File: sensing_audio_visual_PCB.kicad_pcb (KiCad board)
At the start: 2 copper layers, 52 x 41.4 mm, 0 parts

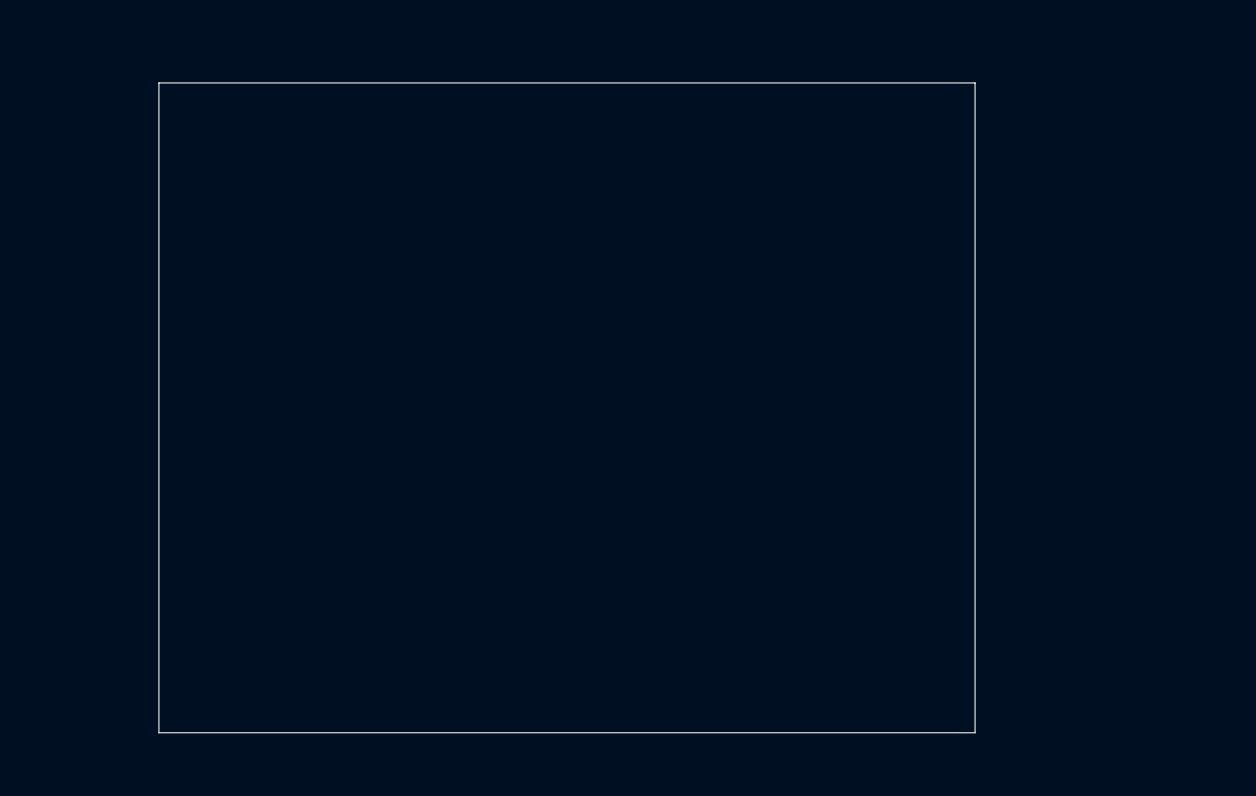
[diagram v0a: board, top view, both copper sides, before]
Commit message: Footprints added
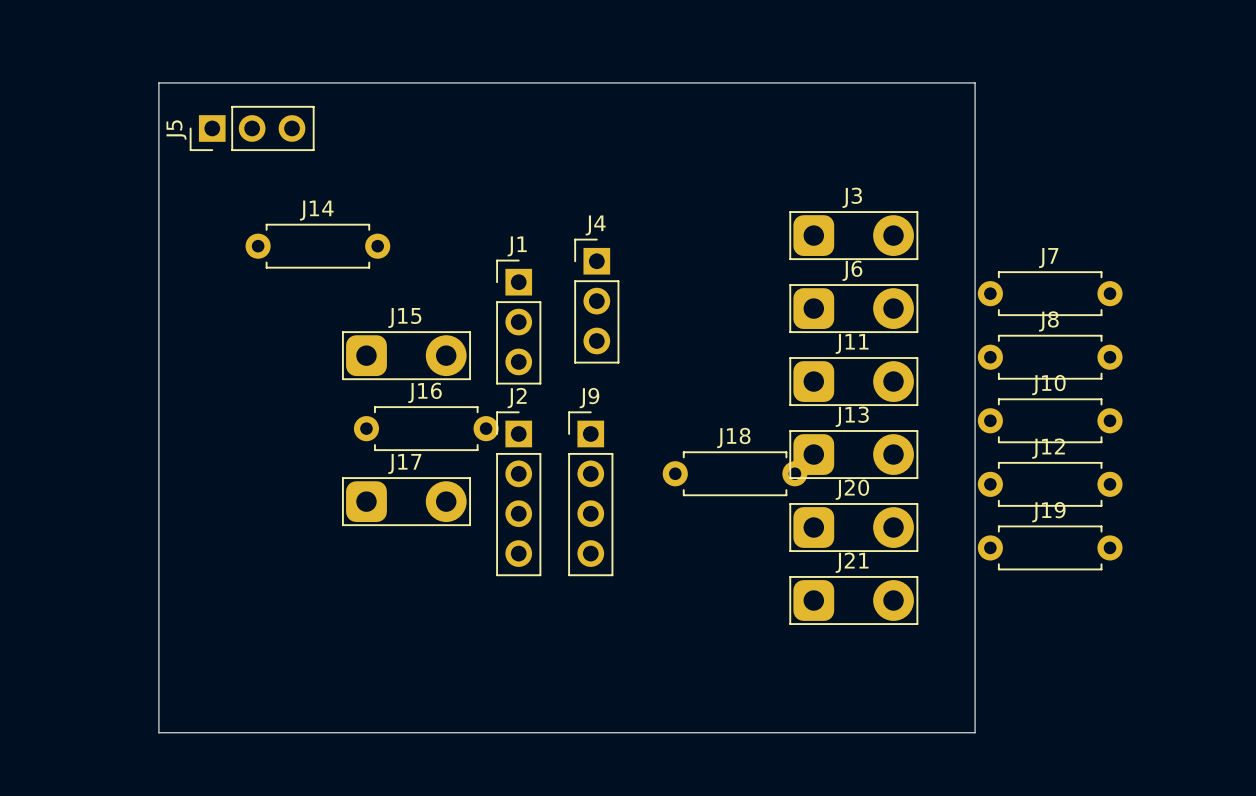
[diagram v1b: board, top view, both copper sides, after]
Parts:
- added J1: Amplifier, Connector_PinHeader_2.54mm:PinHeader_1x03_P2.54mm_Vertical, F.Cu at (124.5, 77.3)
- added J10: 220 ohm, Resistor_THT:R_Axial_DIN0207_L6.3mm_D2.5mm_P7.62mm_Horizontal, F.Cu at (154.6, 86.1)
- added J11: IR Emitter, TestPoint:TestPoint_2Pads_Pitch5.08mm_Drill1.3mm, F.Cu at (143.3, 83.6)
- added J12: 10k ohm, Resistor_THT:R_Axial_DIN0207_L6.3mm_D2.5mm_P7.62mm_Horizontal, F.Cu at (154.6, 90.2)
- added J13: IR Receiver, TestPoint:TestPoint_2Pads_Pitch5.08mm_Drill1.3mm, F.Cu at (143.3, 88.3)
- added J14: 220 ohm, Resistor_THT:R_Axial_DIN0207_L6.3mm_D2.5mm_P7.62mm_Horizontal, F.Cu at (107.9, 75.0)
- added J15: IR Emitter, TestPoint:TestPoint_2Pads_Pitch5.08mm_Drill1.3mm, F.Cu at (114.8, 82.0)
- added J16: 10k ohm, Resistor_THT:R_Axial_DIN0207_L6.3mm_D2.5mm_P7.62mm_Horizontal, F.Cu at (114.8, 86.6)
- added J17: IR Receiver, TestPoint:TestPoint_2Pads_Pitch5.08mm_Drill1.3mm, F.Cu at (114.8, 91.3)
- added J18: 220 ohm, Resistor_THT:R_Axial_DIN0207_L6.3mm_D2.5mm_P7.62mm_Horizontal, F.Cu at (134.5, 89.5)
- added J19: 10k ohm, Resistor_THT:R_Axial_DIN0207_L6.3mm_D2.5mm_P7.62mm_Horizontal, F.Cu at (154.6, 94.2)
- added J2: OLED Display, Connector_PinHeader_2.54mm:PinHeader_1x04_P2.54mm_Vertical, F.Cu at (124.5, 87.0)
- added J20: IR Emitter, TestPoint:TestPoint_2Pads_Pitch5.08mm_Drill1.3mm, F.Cu at (143.3, 92.9)
- added J21: IR Receiver, TestPoint:TestPoint_2Pads_Pitch5.08mm_Drill1.3mm, F.Cu at (143.3, 97.6)
- added J3: IR Emitter, TestPoint:TestPoint_2Pads_Pitch5.08mm_Drill1.3mm, F.Cu at (143.3, 74.3)
- added J4: Light Strip, Connector_PinHeader_2.54mm:PinHeader_1x03_P2.54mm_Vertical, F.Cu at (129.5, 76.0)
- added J5: Conn_01x03, Connector_PinHeader_2.54mm:PinHeader_1x03_P2.54mm_Vertical, F.Cu at (105.0, 67.5)
- added J6: IR Receiver, TestPoint:TestPoint_2Pads_Pitch5.08mm_Drill1.3mm, F.Cu at (143.3, 79.0)
- added J7: 220 ohm, Resistor_THT:R_Axial_DIN0207_L6.3mm_D2.5mm_P7.62mm_Horizontal, F.Cu at (154.6, 78.0)
- added J8: 10k ohm, Resistor_THT:R_Axial_DIN0207_L6.3mm_D2.5mm_P7.62mm_Horizontal, F.Cu at (154.6, 82.1)
- added J9: GPIO Pins, Connector_PinHeader_2.54mm:PinHeader_1x04_P2.54mm_Vertical, F.Cu at (129.1, 87.0)

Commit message: Layout finished
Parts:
- added J22: R_PhotoR, Resistor_THT:R_Axial_DIN0207_L6.3mm_D2.5mm_P7.62mm_Horizontal, F.Cu at (138.3, 74.0)
- added J23: photoresistor, TestPoint:TestPoint_2Pads_Pitch5.08mm_Drill1.3mm, F.Cu at (123.5, 74.0)
- added J25: R_PhotoR, Resistor_THT:R_Axial_DIN0207_L6.3mm_D2.5mm_P7.62mm_Horizontal, F.Cu at (158.2, 74.0)
- added J26: photoresistor, TestPoint:TestPoint_2Pads_Pitch5.08mm_Drill1.3mm, F.Cu at (151.0, 74.0)
- added J27: R_LED, Resistor_THT:R_Axial_DIN0207_L6.3mm_D2.5mm_P7.62mm_Horizontal, F.Cu at (158.7, 81.0)
- added J28: LED, TestPoint:TestPoint_2Pads_Pitch5.08mm_Drill1.3mm, F.Cu at (165.5, 88.5)
- added J29: R_LED, Resistor_THT:R_Axial_DIN0207_L6.3mm_D2.5mm_P7.62mm_Horizontal, F.Cu at (158.5, 95.5)
- added J30: LED, TestPoint:TestPoint_2Pads_Pitch5.08mm_Drill1.3mm, F.Cu at (155.5, 104.0)
- added REF**: MountingHole_3.2mm_M3, MountingHole:MountingHole_3.2mm_M3, F.Cu at (99.0, 67.0)
- added REF**: MountingHole_3.2mm_M3, MountingHole:MountingHole_3.2mm_M3, F.Cu at (164.0, 103.0)
- added REF**: MountingHole_3.2mm_M3, MountingHole:MountingHole_3.2mm_M3, F.Cu at (99.0, 103.0)
- added REF**: MountingHole_3.2mm_M3, MountingHole:MountingHole_3.2mm_M3, F.Cu at (164.0, 66.5)
- J10, J14, J18, J7: value 220 ohm -> R_emitter
- J12, J16, J19, J8: value 10k ohm -> R_receiver
- J9: value GPIO Pins -> Conn_01x06; footprint Connector_PinHeader_2.54mm:PinHeader_1x04_P2.54mm_Vertical -> Connector_PinHeader_2.54mm:PinHeader_1x06_P2.54mm_Vertical
- moved J7 52.9 mm to (104.7, 95.5)
- moved J11 47.0 mm to (98.0, 96.0), turned to 90 degrees
- moved J10 42.9 mm to (115.3, 103.5), turned to 180 degrees
- moved J20 34.1 mm to (109.6, 88.2), turned to 180 degrees
- moved J16 33.8 mm to (143.8, 104.0), turned to 180 degrees
- moved J3 32.2 mm to (119.1, 95.5)
- moved J2 29.2 mm to (98.0, 74.7)
- moved J1 25.5 mm to (147.4, 66.0), turned to 90 degrees
- moved J4 25.3 mm to (104.2, 74.0), turned to 90 degrees
- moved J12 25.1 mm to (131.2, 81.0)
- moved J19 23.4 mm to (131.2, 95.5)
- moved J9 21.3 mm to (125.4, 66.0), turned to 90 degrees
- moved J17 18.0 mm to (127.5, 104.0), turned to 180 degrees
- moved J6 11.4 mm to (137.0, 88.5), turned to 180 degrees
- moved J18 9.83 mm to (124.8, 88.2), turned to 180 degrees
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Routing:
- net /5V: track 0.00 -> 84.4 mm
- net /GND: track 0.00 -> 50.0 mm, vias 0 -> 16
- net Net-(J16-Pin_2): track 0.00 -> 47.5 mm
- net Net-(J19-Pin_2): track 0.00 -> 44.8 mm
- net /3V3: track 0.00 -> 35.0 mm, vias 0 -> 11
- net Net-(J25-Pin_2): track 0.00 -> 34.1 mm
- net Net-(J6-Pin_1): track 0.00 -> 32.5 mm
- net Net-(J12-Pin_2): track 0.00 -> 24.9 mm
- net Net-(J22-Pin_2): track 0.00 -> 17.2 mm
- net Net-(J29-Pin_2): track 0.00 -> 14.1 mm
- net Net-(J10-Pin_2): track 0.00 -> 12.8 mm
- net Net-(J27-Pin_2): track 0.00 -> 8.03 mm
- net Net-(J18-Pin_2): track 0.00 -> 7.55 mm
- net Net-(J14-Pin_2): track 0.00 -> 6.75 mm
- net Net-(J3-Pin_1): track 0.00 -> 6.56 mm
- added copper zone on F.Cu, net /3V3
- added copper zone on B.Cu, net /GND
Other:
- board size 52 x 41.4 mm -> 76 x 46.5 mm

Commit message: Layout finished
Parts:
- GPIO Pins 1, 2, 3, 4, 5, 6: renamed from J9
- IR Emitter: renamed from J20
- IR Emitter: renamed from J11
- IR Emitter: renamed from J3
- IR Emitter: renamed from J15
- IR Receiver 1: renamed from J17
- IR Receiver 2: renamed from J21
- IR Receiver 3: renamed from J6
- IR Receiver 4: renamed from J13
- Light Strip: renamed from J4
- OLED Display: renamed from J2
- Photoresistor 5: renamed from J23
- Photoresistor 6: renamed from J26
- Power & GND: renamed from J5
- R_for_emitter: renamed from J18; value R_emitter -> R_for_emitter
- R_for_emitter: renamed from J10; value R_emitter -> R_for_emitter
- moved Amplifier 0.50 mm to (147.4, 66.5)
- renumbered J1 to Amplifier, J28 to LED, J30 to LED, J27 to R_for_LED, J29 to R_for_LED, J22 to R_for_PhotoR, J25 to R_for_PhotoR, J7 to R_for_emitter, J14 to R_for_emitter, J8 to R_for_receiver, J12 to R_for_receiver, J16 to R_for_receiver, J19 to R_for_receiver
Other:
- board text added: "SCL"
- board text added: "SDA"
- board text added: "SecA_Team 8 BuzzKill"
